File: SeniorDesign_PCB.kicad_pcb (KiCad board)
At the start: 4 copper layers, 128.2 x 50.4 mm, 193 parts, among them J1 Conn_01x04_Pin, J10 Conn_01x02_Socket, J11 Conn_01x02_Pin, J12 USB_C_Receptacle_USB2.0_14P, J13 USB_C_Receptacle_USB2.0_14P, J14 IDC_Cable_02x08, J15 Conn_01x02_Pin, J16 Conn_01x04_Pin, J17 Conn_01x04_Pin, J18 Micro_SD_Card, J19 Conn_01x02_Socket, J2 Conn_01x02_Socket, J20 Conn_01x02_Socket, J21 MIC_I2S_CONNECTOR, J22 Conn_01x02_Socket, J23 Conn_01x02_Socket, J24 Conn_01x02_Socket, J3 Conn_01x03_Socket, J4 Conn_01x04_Pin, J5 Conn_01x02_Pin, J6 Conn_01x02_Socket, J7 Conn_01x02_Socket, J8 Conn_01x02_Socket, Q1 NMOS, Q2 NMOS, Q4 AO3400A, Q5 AO3400A, SW2 SW_Push, SW5 SW_Push, SW6 SW_Push, SW7 SW_Push, U1 TMP117xxDRV, U10 INA219AxD, U11 TLV62569ADRL, U12 USBLC6-2P6, U13 USBLC6-2P6, U14 ESP32-C3FH4, U15 TPS60400DBV, U16 TLV172IDCK, U2 RV-3028-C7, U3 STM32G474RETx, U5 MAX98357A, U6 TLV172IDCK, U7 TLV172IDCK, U8 MAX98357A, U9 INA219AxD, Y1 16MHz, Y2 40MHz

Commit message: layout
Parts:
- removed C20: 4u7, Capacitor_SMD:C_0603_1608Metric
- removed C21: 22u, Capacitor_SMD:C_0603_1608Metric
- removed C51, C54, C55: DNP, Capacitor_SMD:C_0603_1608Metric
- removed D10: D, Diode_SMD:D_1206_3216Metric
- removed D5: LED, LED_SMD:LED_0603_1608Metric
- removed L1: 1u, Inductor_SMD:L_Bourns-SRN8040_8x8.15mm
- removed R15: 10k, Resistor_SMD:R_0603_1608Metric
- removed R40: 453k, Resistor_SMD:R_0603_1608Metric
- removed R41: 100k, Resistor_SMD:R_0603_1608Metric
- removed R42: 2m, Resistor_SMD:R_0603_1608Metric
- removed R43: 330, Resistor_SMD:R_0603_1608Metric
- removed R44: 5k1, Resistor_SMD:R_0603_1608Metric
- removed U11: TLV62569ADRL, Package_TO_SOT_SMD:SOT-563
- added C56: 22u, Capacitor_SMD:C_0805_2012Metric, F.Cu at (51.1, 3.88)
- added C57: 100n, Capacitor_SMD:C_0603_1608Metric, F.Cu at (14.3, 6.64)
- added C58: 330p, Capacitor_SMD:C_0603_1608Metric, F.Cu at (14.3, 9.15)
- added C59: 330p, Capacitor_SMD:C_0603_1608Metric, F.Cu at (14.3, 11.7)
- added C60: 2u2, Capacitor_SMD:C_0603_1608Metric, F.Cu at (14.3, 14.2)
- added C61: 22u, Capacitor_SMD:C_1210_3225Metric, F.Cu at (45.9, 15.4)
- added C62: 22u, Capacitor_SMD:C_1210_3225Metric, F.Cu at (45.9, 19.7)
- added C63: 22u, Capacitor_SMD:C_1210_3225Metric, F.Cu at (45.9, 23.9)
- added C64: 100n, Capacitor_SMD:C_0603_1608Metric, F.Cu at (14.3, 16.7)
- added C65: 1u, Capacitor_SMD:C_0603_1608Metric, F.Cu at (14.3, 19.2)
- added C66: 100n, Capacitor_SMD:C_0603_1608Metric_Pad1.08x0.95mm_HandSolder, F.Cu at (56.2, -10.2)
- added C72: 100n, Capacitor_SMD:C_0603_1608Metric_Pad1.08x0.95mm_HandSolder, F.Cu at (56.2, -7.74)
- added C73: 82p, Capacitor_SMD:C_0603_1608Metric_Pad1.08x0.95mm_HandSolder, F.Cu at (56.2, -5.22)
- added C74: 47u, Capacitor_SMD:C_1210_3225Metric, F.Cu at (45.9, 28.2)
- added C75: 100n, Capacitor_SMD:C_0603_1608Metric_Pad1.08x0.95mm_HandSolder, F.Cu at (56.2, -2.71)
- added C76: DNP, Capacitor_SMD:C_1210_3225Metric, F.Cu at (45.9, 32.4)
- added C77: 15u, Capacitor_SMD:C_1210_3225Metric, F.Cu at (45.9, 36.7)
- added C78: DNP, Package_TO_SOT_SMD:SOT-23-6, F.Cu at (51.5, -9.10)
- added C79: DNP, Capacitor_SMD:C_0603_1608Metric_Pad1.08x0.95mm_HandSolder, F.Cu at (56.2, -0.20)
- added D1: ESDA25P35-1U1M, ESDA25P35-1U1M:ESDA25P351U1M, F.Cu at (56.5, 3.10)
- added D11: LED, LED_SMD:LED_0603_1608Metric, F.Cu at (45.1, 40.1)
- added H1: MountingHole, MountingHole:MountingHole_3.2mm_M3, F.Cu at (12.2, 48.0)
- added H2: MountingHole, MountingHole:MountingHole_3.2mm_M3, F.Cu at (12.2, 56.0)
- added H3: MountingHole, MountingHole:MountingHole_3.2mm_M3, F.Cu at (12.2, 63.9)
- added H4: MountingHole, MountingHole:MountingHole_3.2mm_M3, F.Cu at (12.2, 71.9)
- added J25: Conn_01x02_Socket, Connector_PinHeader_2.54mm:PinHeader_1x02_P2.54mm_Vertical, F.Cu at (46.6, -9.21)
- added J26: Conn_01x08_Socket, Connector_PinHeader_2.54mm:PinHeader_1x08_P2.54mm_Vertical, F.Cu at (172.0, 72.1)
- added J27: Conn_01x02_Socket, Connector_PinHeader_2.54mm:PinHeader_1x02_P2.54mm_Vertical, F.Cu at (42.5, 79.9)
- added J9: Conn_01x08_Socket, Connector_PinHeader_2.54mm:PinHeader_1x08_P2.54mm_Vertical, F.Cu at (156.4, 72.1)
- added L10: 1.5u, Inductor_SMD:IHLP5050EZER1R5M01, F.Cu at (10.8, 33.5)
- added Q6: NMOS, Package_TO_SOT_SMD:TSOT-23, F.Cu at (37.8, -1.92)
- added Q7: NMOS, Package_TO_SOT_SMD:TSOT-23, F.Cu at (37.8, 2.75)
- added R1: 100k, Resistor_SMD:R_0603_1608Metric, F.Cu at (14.3, 21.7)
- added R16: 1k, Resistor_SMD:R_0603_1608Metric, F.Cu at (14.3, 24.2)
- added R4: 10k, Resistor_SMD:R_0402_1005Metric, F.Cu at (58.6, 24.3)
- added R63: 73.2k, Resistor_SMD:R_0402_1005Metric, F.Cu at (58.6, 26.3)
- added R64: 10k, Resistor_SMD:R_0603_1608Metric, F.Cu at (22.3, 6.64)
- added R65: 560, Resistor_SMD:R_0603_1608Metric, F.Cu at (22.3, 9.15)
- added R66: 10m, Resistor_SMD:R_1206_3216Metric, F.Cu at (58.3, 10.4)
- added R67: 22k, Resistor_SMD:R_0603_1608Metric, F.Cu at (22.3, 11.7)
- added R77: 330, Resistor_SMD:R_0603_1608Metric, F.Cu at (26.3, 14.2)
- added R86: DNP, Resistor_SMD:R_1210_3225Metric_Pad1.30x2.65mm_HandSolder, F.Cu at (43.5, -2.25)
- added R87: 2m, Resistor_SMD:R_0603_1608Metric, F.Cu at (26.3, 16.7)
- added R88: 0R, Resistor_SMD:R_1210_3225Metric_Pad1.30x2.65mm_HandSolder, F.Cu at (43.5, 1.96)
- added U17: TCPP03-M20, Package_DFN_QFN:TQFN-20-1EP_4x4mm_P0.5mm_EP2.1x2.1mm, F.Cu at (31.8, 38.9)
- added U18: TPS54302, Package_TO_SOT_SMD:SOT-23-6, F.Cu at (51.5, 0.15)
- added U4: TPS513885VABR, TPS513885VABR:VAB0013A-MFG, F.Cu at (38.0, 38.5)
- C1, C10, C12, C13, C16, C17, C19, C2, C3, C32, C33, C34, C35, C36, C37, C38, C39, C4, C40, C41, C43, C44, C46, C47, C48, C49, C5, C50, C52, C53, C6, C7, D8, L4, Q2, R2, R45, R47, R5, R52, R53, R6, R61, R62, R7, R74, R75, R8, R82, R85, U10, U15: moved to F.Cu
- C28, C29: footprint Capacitor_SMD:C_0402_1005Metric -> Capacitor_SMD:C_0201_0603Metric_Pad0.64x0.40mm_HandSolder
- C30: value DNP -> 100n; footprint Capacitor_SMD:C_0402_1005Metric -> Capacitor_SMD:C_0603_1608Metric
- C31: value DNP -> 470pF
- L2: footprint Inductor_SMD:L_0402_1005Metric -> Inductor_SMD:L_0201_0603Metric_Pad0.64x0.40mm_HandSolder
- L3: value DNP -> 10u; footprint Inductor_SMD:L_0402_1005Metric -> Inductor_SMD:L_12x12mm_H6mm
- R10: value 10k -> 3.3k; moved to F.Cu
- R46: value 5k1 -> 100k; moved to F.Cu
- R72: value DNP -> 0R; moved to F.Cu
- R73: value 0R -> DNP; moved to F.Cu
- R9: value 7k -> 17k; moved to F.Cu
- moved J22 200.3 mm to (37.4, -9.21)
- moved J23 193.4 mm to (42.0, -9.21)
- moved C19 187.0 mm to (10.3, 9.15)
- moved R32 186.9 mm to (18.3, 9.15), turned to 0 degrees
- moved R31 186.6 mm to (18.3, 6.64), turned to 0 degrees
- moved C18 179.1 mm to (10.3, 6.64), turned to 0 degrees
- moved R38 178.8 mm to (18.3, 11.7), turned to 0 degrees
- moved R39 174.6 mm to (18.3, 14.2), turned to 0 degrees
- moved R73 167.1 mm to (26.3, 6.64), turned to 0 degrees
- moved J19 166.9 mm to (66.5, 0.72)
- moved R46 165.6 mm to (18.3, 16.7), turned to 0 degrees
- moved R74 163.1 mm to (26.3, 9.15), turned to 0 degrees
- moved R61 162.8 mm to (18.3, 24.2), turned to 0 degrees
- moved R75 162.6 mm to (26.3, 11.7)
- moved R72 162.1 mm to (22.3, 24.2)
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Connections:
- net /Peripherials/STM32_USB_D_N renamed /Power/STM32_USB_D_N
- net /Peripherials/STM32_USB_D_P renamed /Power/STM32_USB_D_P
- net /Peripherials/USB_N_STM_ESD renamed /Power/USB_N_STM_ESD
- net /Peripherials/USB_N_STM_RES renamed /Power/USB_N_STM_RES
- net /Peripherials/USB_P_STM_ESD renamed /Power/USB_P_STM_ESD
- net /Peripherials/USB_P_STM_RES renamed /Power/USB_P_STM_RES
- C29 pad 1: /ESP32C3/L_to_L -> /ESP32C3/LNA_IN
- C30 pad 1: /ESP32C3/L_to_L -> Net-(U4-VBST)
- C30 pad 2: GND -> Net-(C30-Pad2)
- C31 pad 1: /ESP32C3/LNA_IN -> Net-(C31-Pad1)
- C31 pad 2: GND -> +5V
- J12 pad A4: /Peripherials/VBUS_STM -> /Power/VBUS_STM
- J12 pad A9: /Peripherials/VBUS_STM -> /Power/VBUS_STM
- J12 pad B4: /Peripherials/VBUS_STM -> /Power/VBUS_STM
- J12 pad B9: /Peripherials/VBUS_STM -> /Power/VBUS_STM
- L2 pad 2: /ESP32C3/L_to_L -> /ESP32C3/LNA_IN
- L3 pad 1: /ESP32C3/L_to_L -> Net-(U18-SW)
- L3 pad 2: /ESP32C3/LNA_IN -> /Power/3V3_AMPS_1
- R12 pad 1: /STM32G4/SPI1_MOSI_0 -> /ESP32C3/SPI1_MOSI
- R13 pad 1: /STM32G4/SPI1_MISO_0 -> /ESP32C3/SPI1_MISO
- R14 pad 1: /STM32G4/SPI1_SCLK_0 -> /ESP32C3/SPI1_SCLK
- R46 pad 1: GND -> /Power/3V3_AMPS_1
- R46 pad 2: Net-(J12-CC1) -> Net-(U18-FB)
- R9 pad 1: /Peripherials/VBUS_STM -> /Power/VBUS_STM
- U12 pad 5: /Peripherials/VBUS_STM -> /Power/VBUS_STM
- U3 pad 17: /Power/5V_VOLTS -> /Power/I_ANA
- U3 pad 18: /STM32G4/3V3_VOLTS -> /Peripherials/SPI_CS_ESPMini
- U3 pad 19: /STM32G4/SPI1_SCLK_0 -> /ESP32C3/SPI1_SCLK
- U3 pad 20: /STM32G4/SPI1_MISO_0 -> /ESP32C3/SPI1_MISO
- U3 pad 21: /STM32G4/SPI1_MOSI_0 -> /ESP32C3/SPI1_MOSI
- U3 pad 3: unconnected-(U3-PC14-Pad3) -> /Peripherials/MATRIX_R1
- U3 pad 4: unconnected-(U3-PC15-Pad4) -> /Peripherials/MATRIX_C
- U3 pad 55: unconnected-(U3-PD2-Pad55) -> /Power/PD_EN
- U3 pad 57: /Peripherials/MATRIX_C -> /Power/USBPD_CC2
- U3 pad 59: /Peripherials/MATRIX_R1 -> /Power/USBPD_CC1
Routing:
- net 3V3: track 140.6 -> 0.00 mm, vias 37 -> 0
- net 5V: track 107.1 -> 0.00 mm, vias 6 -> 0
- net /Power/I2C3_SCL: track 106.6 -> 0.00 mm, vias 4 -> 0
- net /ESP32C3/SPI1_MISO: track 101.5 -> 0.00 mm, vias 4 -> 0
- net USB_5V: track 99.2 -> 0.00 mm, vias 7 -> 0
- net /ESP32C3/SPI1_MOSI: track 87.9 -> 0.00 mm, vias 4 -> 0
- net /ESP32C3/SPI1_SCLK: track 81.6 -> 0.00 mm, vias 4 -> 0
- net /Power/I2C3_SDA: track 78.2 -> 0.00 mm, vias 3 -> 0
- net /ESP32C3/SPI1_CS_ESP: track 71.8 -> 0.00 mm, vias 2 -> 0
- net /STM32G4/I2S3_CK: track 57.5 -> 0.00 mm, vias 1 -> 0
- net /STM32G4/I2S3_WS: track 55.1 -> 0.00 mm, vias 1 -> 0
- net /Analog/LEFT_SD_MODE: track 55.1 -> 0.00 mm, vias 2 -> 0
- net /STM32G4/I2S3_SD: track 54.2 -> 0.00 mm, vias 1 -> 0
- net /ESP32C3/ESP32_RST: track 50.6 -> 0.00 mm
- net /STM32G4/nRST: track 49.6 -> 0.00 mm
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- removed copper zone on F.Cu, net /Power/5V_AMPS_1
- removed copper zone on In2.Cu, net 3V3
- removed copper zone on F.Cu, net 5V
- removed copper zone on B.Cu, net GND
- removed copper zone on In1.Cu, net GND
- removed copper zone on F.Cu, net Net-(J10-Pin_1)
- removed copper zone on F.Cu, net Net-(J24-Pin_2)
- removed copper zone on B.Cu, net Net-(U11-SW)
- removed copper zone on B.Cu, net USB_5V
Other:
- board outline removed
- board text removed: "3V3"
- board text removed: "A"
- board text removed: "ALS"
- board text removed: "BOOT0"
- board text removed: "CK"
- board text removed: "DISPLAY"
- board text removed: "FAN"
- board text removed: "GND"
- board text removed: "K"
- board text removed: "MASHED PCB"
- board text removed: "MIC"
- board text removed: "NRST"
- board text removed: "PIR"
- board text removed: "PWR"
- board text removed: "SCL"
- board text removed: "SD"
- board text removed: "SDA"
- board text removed: "SWCLK"
- board text removed: "TEAM 20"
- board text removed: "V1 Rev0"
- board text removed: "WS"

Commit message: taking a break
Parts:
- C30, C31, C56, C61, C62, C63, C64, C65, C66, C72, C73, C74, C75, C76, C77, C78, C79, D11, L3, R1, R16, R4, R46, R63, R67, R77, R86, R87, R88, U18, U4: moved to B.Cu
- moved R46 277.3 mm to (292.9, 55.3), turned to 180 degrees
- moved R67 269.4 mm to (288.9, 50.3), turned to 180 degrees
- moved R77 261.4 mm to (284.9, 52.8), turned to 180 degrees
- moved R87 261.4 mm to (284.9, 55.3), turned to 180 degrees
- moved L3 242.9 mm to (275.5, 59.1), turned to 180 degrees
- moved R86 227.9 mm to (265.7, 48.5), turned to 180 degrees
- moved R88 227.9 mm to (265.7, 52.8), turned to 180 degrees
- moved L10 225.5 mm to (234.1, 65.4)
- moved D11 224.3 mm to (266.0, 78.7), turned to 180 degrees
- moved C30 224.0 mm to (232.9, 35.6), turned to 180 degrees
- moved C74 222.7 mm to (265.3, 66.8), turned to 180 degrees
- moved C76 222.7 mm to (265.3, 71.1), turned to 180 degrees
- moved C77 222.7 mm to (265.3, 75.3), turned to 180 degrees
- moved R16 217.6 mm to (231.2, 41.2), turned to 180 degrees
- moved R1 217.3 mm to (229.6, 50.6), turned to 180 degrees
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
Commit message: just keep swimming
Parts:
- moved C43 111.0 mm to (116.9, 45.0), turned to 180 degrees
- moved C50 107.5 mm to (116.6, 39.5)
- moved C48 106.5 mm to (113.9, 43.5), turned to -90 degrees
- moved C49 105.2 mm to (113.9, 40.0), turned to 90 degrees
- moved C47 105.1 mm to (111.9, 43.5), turned to -90 degrees
- moved U15 80.8 mm to (117.3, 42.4)
- moved U7 52.2 mm to (126.7, 37.2)
- moved C44 45.2 mm to (126.9, 34.7), turned to 180 degrees
- moved C53 44.8 mm to (116.2, 23.6), turned to 180 degrees
- moved R28 44.0 mm to (125.9, 40.2), turned to 90 degrees
- moved R29 43.0 mm to (128.4, 39.7), turned to 180 degrees
- moved C15 40.3 mm to (114.6, 36.6)
- moved R21 40.3 mm to (113.8, 34.2)
- moved R22 40.3 mm to (116.2, 35.0)
- moved R26 40.3 mm to (123.8, 37.2)
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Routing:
- net -3V3: track 0.00 -> 27.0 mm
- net 3V3: track 0.00 -> 9.95 mm
- net Net-(J6-Pin_2): track 0.00 -> 7.53 mm
- net Net-(J7-Pin_2): track 0.00 -> 4.69 mm
- net Net-(U16-+): track 0.00 -> 4.63 mm
- net Net-(J8-Pin_2): track 0.00 -> 4.60 mm
- net Net-(J8-Pin_1): track 0.00 -> 4.45 mm
- net /ESP32C3/SPI1_SCLK: track 0.00 -> 4.42 mm
- net Net-(J7-Pin_1): track 0.00 -> 4.36 mm
- net Net-(U6--): track 0.00 -> 4.05 mm
- net Net-(U15-C_{FLY+}): track 0.00 -> 4.02 mm
- net /ESP32C3/SPI1_MISO: track 0.00 -> 3.60 mm
- net Net-(R23-Pad2): track 0.00 -> 3.53 mm
- net Net-(U16--): track 0.00 -> 3.49 mm
- net Net-(U7--): track 0.00 -> 3.33 mm
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
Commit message: grouped hitngs
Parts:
- C41, L10: moved to B.Cu
- moved C41 158.3 mm to (188.4, 73.6)
- moved C57 140.9 mm to (58.6, 140.4)
- moved D1 140.4 mm to (51.0, 143.4)
- moved C58 137.1 mm to (52.6, 140.8), turned to 180 degrees
- moved C60 136.6 mm to (51.0, 145.8), turned to 180 degrees
- moved Q6 135.0 mm to (47.1, 132.8), turned to 180 degrees
- moved C59 134.6 mm to (58.6, 138.8)
- moved Q7 133.9 mm to (47.1, 136.3), turned to 180 degrees
- moved R65 132.9 mm to (50.6, 139.0), turned to 180 degrees
- moved R64 132.9 mm to (51.0, 136.4), turned to -90 degrees
- moved R66 130.9 mm to (47.6, 140.8), turned to -90 degrees
- moved R48 130.5 mm to (54.6, 144.6), turned to 90 degrees
- moved R49 128.6 mm to (56.4, 144.6), turned to 90 degrees
- moved C52 118.9 mm to (188.8, 33.8)
- moved J12 109.0 mm to (54.3, 150.6)
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
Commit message: ESP32 Routing
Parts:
- C28, C29: footprint Capacitor_SMD:C_0201_0603Metric_Pad0.64x0.40mm_HandSolder -> Capacitor_SMD:C_0402_1005Metric_Pad0.74x0.62mm_HandSolder
- C32, C34, C35, C37, C39: moved to B.Cu
- L2: footprint Inductor_SMD:L_0201_0603Metric_Pad0.64x0.40mm_HandSolder -> Inductor_SMD:L_0402_1005Metric_Pad0.77x0.64mm_HandSolder
- moved R10 250.8 mm to (-72.9, 134.6)
- moved R5 250.8 mm to (-72.9, 127.1)
- moved R9 250.8 mm to (-72.9, 132.1)
- moved C11 250.8 mm to (-78.0, 132.2)
- moved R17 250.8 mm to (-68.9, 132.1)
- moved R11 250.8 mm to (-72.9, 137.1)
- moved R6 250.8 mm to (-72.9, 129.6)
- moved C42 249.5 mm to (-47.8, 142.1)
- moved C6 249.5 mm to (-27.3, 152.3)
- moved C9 249.5 mm to (-46.7, 160.3)
- moved R12 249.5 mm to (-37.3, 166.3)
- moved R13 249.5 mm to (-38.9, 166.3)
- moved R14 249.5 mm to (-40.5, 166.3)
- moved C10 249.5 mm to (-29.1, 150.1)
- moved C4 249.5 mm to (-31.8, 164.9)
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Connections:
- J16 pad 2: /ESP32C3/SPI1_MOSI -> /ESP32C3/SPI1_SCLK
- J16 pad 3: /ESP32C3/SPI1_SCLK -> /ESP32C3/SPI1_MOSI
- J17 pad 1: /ESP32C3/ESP32_RST -> /ESP32C3/GPIO8
- J17 pad 2: /ESP32C3/GPIO8 -> /ESP32C3/ESP32_RST
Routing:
- net /ESP32C3/UART_TX: track 0.00 -> 43.6 mm, vias 0 -> 1
- net /ESP32C3/UART_RX: track 0.00 -> 39.6 mm, vias 0 -> 1
- net /ESP32C3/BOOT: track 0.00 -> 39.1 mm, vias 0 -> 1
- net /ESP32C3/ESP32_RST: track 0.00 -> 31.1 mm, vias 0 -> 1
- net /ESP32C3/GPIO8: track 0.00 -> 22.2 mm
- net 3V3: track 9.47 -> 31.5 mm, vias 0 -> 5
- net Net-(U14-GPIO2): track 0.00 -> 15.6 mm
- net Net-(U14-GPIO10): track 0.00 -> 13.8 mm
- net Net-(U14-GPIO7): track 0.00 -> 13.5 mm
- net Net-(U14-GPIO6): track 0.00 -> 13.4 mm
- net /Peripherials/VBUS_ESP: track 0.00 -> 9.55 mm
- net /ESP32C3/ESP32_USB_D_P: track 0.00 -> 9.19 mm
- net /ESP32C3/ESP32_USB_D_N: track 0.00 -> 8.59 mm
- net /ESP32C3/XTAL_N: track 0.00 -> 7.52 mm
- net /ESP32C3/XTAL_P: track 0.00 -> 7.41 mm
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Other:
- board text added: "600mils"
- board text added: "ESP32-C3"
- board text added: "Test LED"

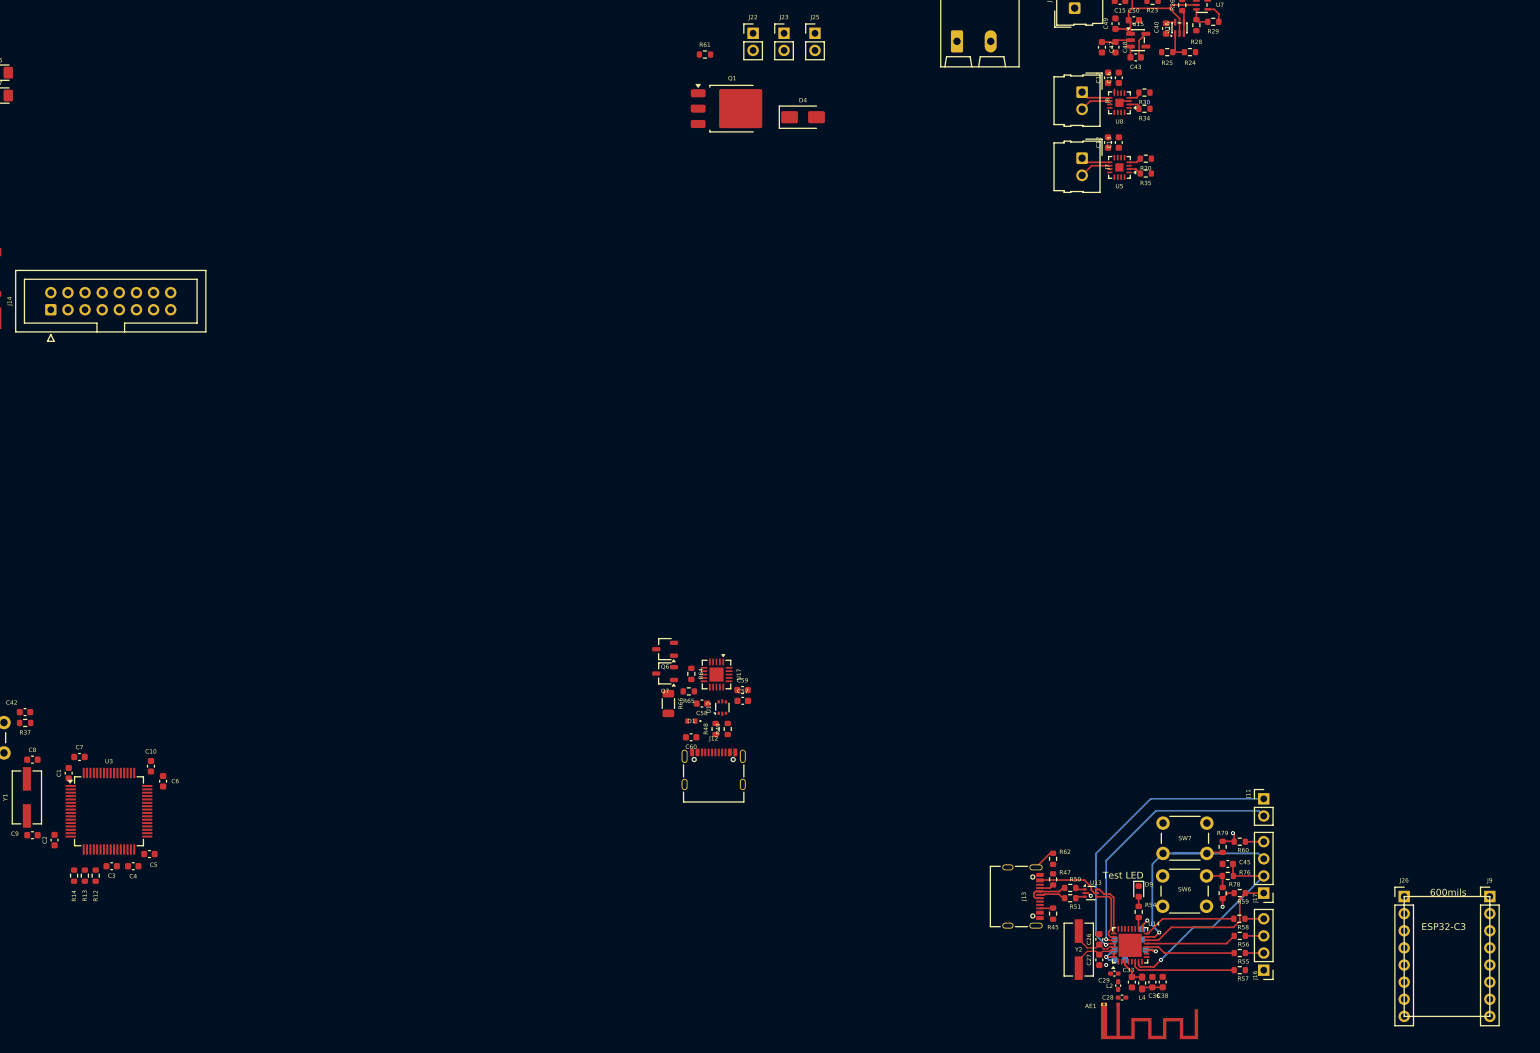
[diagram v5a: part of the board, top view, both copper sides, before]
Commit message: usbpd routing, note that diodes will not work
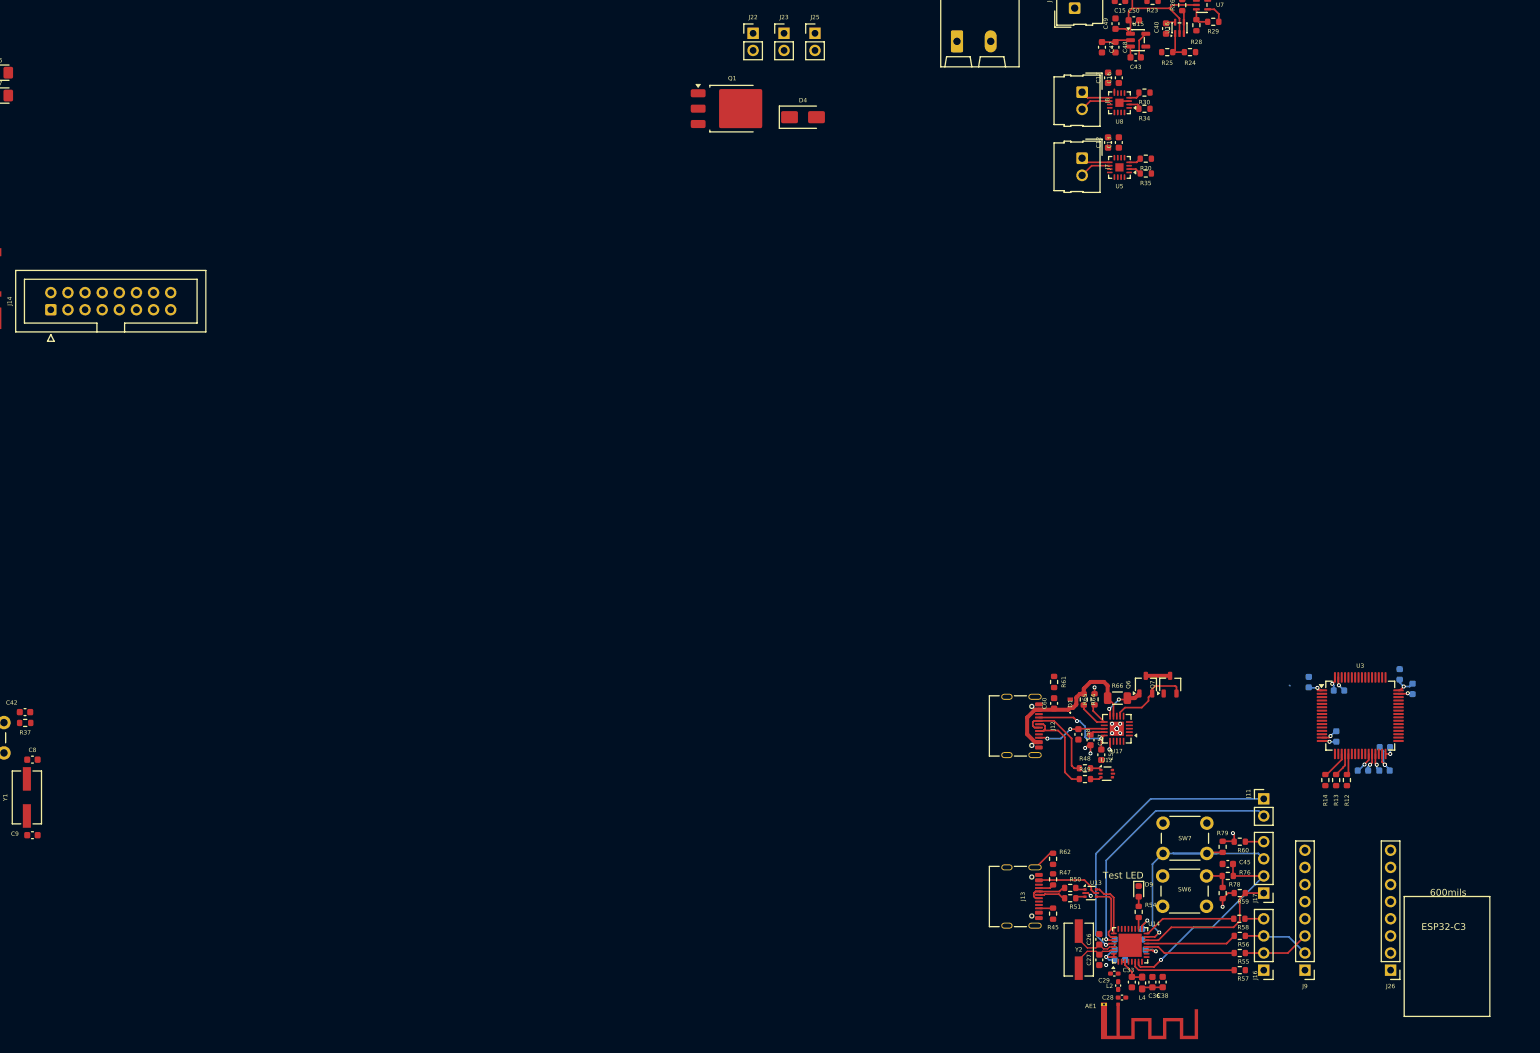
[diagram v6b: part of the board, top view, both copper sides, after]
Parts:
- C1, C10, C2, C3, C4, C5, C6, C7: moved to B.Cu
- moved C2 190.7 mm to (146.7, 145.7)
- moved C7 187.0 mm to (147.1, 138.9)
- moved C4 186.1 mm to (153.8, 150.8)
- moved C3 186.1 mm to (150.6, 150.8)
- moved R12 186.1 mm to (148.2, 152.2)
- moved R13 186.1 mm to (146.6, 152.2)
- moved R14 186.1 mm to (145.0, 152.2)
- moved U3 186.1 mm to (150.2, 142.6)
- moved C6 185.8 mm to (158.0, 138.6)
- moved C10 185.7 mm to (156.1, 136.5)
- moved C1 184.4 mm to (142.6, 137.6)
- moved C5 183.9 mm to (153.8, 147.3), turned to 180 degrees
- moved R61 106.5 mm to (104.8, 137.6), turned to -90 degrees
- moved Q7 74.9 mm to (122.0, 138.0), turned to 90 degrees
- moved Q6 71.5 mm to (118.4, 138.0), turned to 90 degrees
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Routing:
- net /Power/VBUS_STM: track 0.00 -> 25.0 mm
- net GND: track 2.63 -> 23.5 mm, vias 2 -> 22
- net 3V3: track 31.5 -> 48.8 mm, vias 5 -> 12
- net /Power/USB_P_STM_RES: track 0.00 -> 13.9 mm
- net /Power/USB_N_STM_RES: track 0.00 -> 13.8 mm
- net Net-(J12-CC1): track 0.00 -> 13.7 mm, vias 0 -> 2
- net Net-(Q6-G): track 0.00 -> 12.3 mm
- net /ESP32C3/SPI1_SCLK: track 2.73 -> 14.1 mm
- net Net-(J12-CC2): track 0.00 -> 10.3 mm, vias 0 -> 2
- net /ESP32C3/SPI1_MOSI: track 2.73 -> 13.0 mm
- net Net-(U17-V_{sense}): track 0.00 -> 7.63 mm
- net Net-(Q6-D): track 0.00 -> 6.55 mm, vias 0 -> 2
- net Net-(Q6-S): track 0.00 -> 3.60 mm
- net /ESP32C3/SPI1_MISO: track 2.73 -> 6.33 mm
- net Net-(U17-C_{BIAS}): track 0.00 -> 2.40 mm
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
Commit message: saving to not lose prorgress
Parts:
- C28, C29: footprint Capacitor_SMD:C_0402_1005Metric_Pad0.74x0.62mm_HandSolder -> Capacitor_SMD:C_0201_0603Metric_Pad0.64x0.40mm_HandSolder
- L2: footprint Inductor_SMD:L_0402_1005Metric_Pad0.77x0.64mm_HandSolder -> Inductor_SMD:L_0201_0603Metric_Pad0.64x0.40mm_HandSolder
- moved D2 243.5 mm to (160.0, 147.4), turned to 90 degrees
- moved J18 243.4 mm to (165.0, 173.2)
- moved R11 233.0 mm to (160.0, 144.2), turned to -90 degrees
- moved Y1 185.5 mm to (137.4, 139.8)
- moved R24 116.8 mm to (111.0, 160.2), turned to 180 degrees
- moved C15 114.9 mm to (104.0, 151.0)
- moved C43 114.9 mm to (106.3, 159.4)
- moved C47 114.9 mm to (101.3, 157.9)
- moved C48 114.9 mm to (103.3, 157.9)
- moved C49 114.9 mm to (103.3, 154.4)
- moved C50 114.9 mm to (106.0, 153.9)
- moved R21 114.9 mm to (103.2, 148.6)
- moved R22 114.9 mm to (105.6, 149.4)
- moved R23 114.9 mm to (108.8, 151.0)
- moved R26 114.9 mm to (113.2, 151.6)
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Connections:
- J16 pad 2: /ESP32C3/SPI1_SCLK -> /ESP32C3/SPI1_MOSI
- J16 pad 3: /ESP32C3/SPI1_MOSI -> /ESP32C3/SPI1_SCLK
- J17 pad 1: /ESP32C3/GPIO8 -> /ESP32C3/ESP32_RST
- J17 pad 2: /ESP32C3/ESP32_RST -> /ESP32C3/GPIO8
- U3 pad 14: /Peripherials/SPI_CS_SD_CARD -> /Peripherials/MATRIX_LAT
- U3 pad 18: /Peripherials/SPI_CS_ESPMini -> /ESP32C3/SPI1_CS_ESP
- U3 pad 22: /ESP32C3/SPI1_CS_ESP -> /Peripherials/SPI_CS_ESPMini
- U3 pad 33: /Peripherials/MATRIX_LAT -> /Peripherials/SPI_CS_SD_CARD
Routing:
- net /ESP32C3/SPI1_MISO: track 6.33 -> 65.7 mm, vias 0 -> 2
- net /ESP32C3/SPI1_MOSI: track 13.0 -> 68.6 mm, vias 0 -> 1
- net /ESP32C3/SPI1_SCLK: track 14.1 -> 69.1 mm
- net /Peripherials/SPI_CS_ESPMini: track 0.00 -> 24.4 mm, vias 0 -> 1
- net /Peripherials/SPI_CS_SD_CARD: track 0.00 -> 22.6 mm, vias 0 -> 2
- net GND: track 23.5 -> 34.0 mm, vias 22 -> 34
- net /Analog/I2S2_CK: track 0.00 -> 9.57 mm
- net /STM32G4/CLK_IN: track 0.00 -> 9.02 mm
- net /STM32G4/CLK_OUT: track 0.00 -> 7.62 mm
- net 3V3: track 48.8 -> 53.9 mm
- net /STM32G4/TEST_LED: track 0.00 -> 4.12 mm
- net /Analog/I2S2_SD: track 0.00 -> 1.71 mm
- net Net-(D2-A): track 0.00 -> 1.60 mm
